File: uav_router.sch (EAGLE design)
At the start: 6 parts

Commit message: ???
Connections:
- net GND: now also U$1.VSS
- net OSC1: now also Y1.1
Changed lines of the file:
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@@
 <instance part="SUPPLY2" gate="G$1" x="55.88" y="86.36"/>
 <instance part="SUPPLY3" gate="G$1" x="144.78" y="73.66"/>
-<instance part="SUPPLY4" gate="G$1" x="96.52" y="91.44"/>
-<instance part="SUPPLY5" gate="G$1" x="78.74" y="93.98"/>
-<instance part="SUPPLY6" gate="G$1" x="78.74" y="91.44"/>
+<instance part="SUPPLY4" gate="G$1" x="86.36" y="116.84"/>
+<instance part="SUPPLY5" gate="G$1" x="88.9" y="116.84"/>
+<instance part="SUPPLY6" gate="G$1" x="83.82" y="116.84"/>
 <instance part="SUPPLY7" gate="G$1" x="111.76" y="76.2"/>
 <instance part="GND1" gate="1" x="27.94" y="27.94"/>
-<instance part="GND2" gate="1" x="114.3" y="111.76"/>
-<instance part="GND3" gate="1" x="104.14" y="104.14"/>
+<instance part="GND2" gate="1" x="104.14" y="119.38"/>
+<instance part="GND3" gate="1" x="50.8" y="27.94"/>
 <instance part="GND4" gate="1" x="142.24" y="27.94"/>
 <instance part="GND5" gate="1" x="142.24" y="43.18"/>
@@
 <wire x1="33.02" y1="27.94" x2="33.02" y2="91.44" width="0.762" layer="92"/>
 <wire x1="33.02" y1="91.44" x2="35.56" y2="93.98" width="0.762" layer="92"/>
-<wire x1="35.56" y1="93.98" x2="50.8" y2="93.98" width="0.762" layer="92"/>
-<wire x1="50.8" y1="93.98" x2="114.3" y2="93.98" width="0.762" layer="92"/>
+<wire x1="35.56" y1="93.98" x2="48.26" y2="93.98" width="0.762" layer="92"/>
+<wire x1="48.26" y1="93.98" x2="114.3" y2="93.98" width="0.762" layer="92"/>
 <wire x1="114.3" y1="93.98" x2="116.84" y2="91.44" width="0.762" layer="92"/>
-<wire x1="50.8" y1="93.98" x2="48.26" y2="91.44" width="0.762" layer="92"/>
-<wire x1="48.26" y1="91.44" x2="48.26" y2="27.94" width="0.762" layer="92"/>
+<wire x1="48.26" y1="93.98" x2="45.72" y2="91.44" width="0.762" layer="92"/>
+<wire x1="45.72" y1="91.44" x2="45.72" y2="27.94" width="0.762" layer="92"/>
 <wire x1="116.84" y1="91.44" x2="116.84" y2="27.94" width="0.762" layer="92"/>
 <wire x1="114.3" y1="93.98" x2="177.8" y2="93.98" width="0.762" layer="92"/>
@@
 <pinref part="SUPPLY7" gate="G$1" pin="3.3V"/>
 <wire x1="111.76" y1="50.8" x2="111.76" y2="76.2" width="0.1524" layer="91"/>
+<label x="101.6" y="50.8" size="1.778" layer="95"/>
 </segment>
 <segment>
@@
 <pinref part="GND6" gate="1" pin="GND"/>
 <wire x1="111.76" y1="48.26" x2="111.76" y2="30.48" width="0.1524" layer="91"/>
+<label x="101.6" y="48.26" size="1.778" layer="95"/>
 </segment>
 <segment>
@@
 <wire x1="149.86" y1="33.02" x2="142.24" y2="33.02" width="0.1524" layer="91"/>
 <wire x1="142.24" y1="33.02" x2="142.24" y2="30.48" width="0.1524" layer="91"/>
+</segment>
+<segment>
+<pinref part="U$1" gate="G$1" pin="VSS"/>
+<wire x1="60.96" y1="53.34" x2="50.8" y2="53.34" width="0.1524" layer="91"/>
+<wire x1="50.8" y1="53.34" x2="50.8" y2="30.48" width="0.1524" layer="91"/>
+<pinref part="GND3" gate="1" pin="GND"/>
+<label x="53.34" y="53.34" size="1.778" layer="95"/>
 </segment>
 </net>
@@
 <segment>
 <pinref part="U$1" gate="G$1" pin="OSC2"/>
-<wire x1="60.96" y1="48.26" x2="50.8" y2="48.26" width="0.1524" layer="91"/>
-<wire x1="50.8" y1="48.26" x2="48.26" y2="50.8" width="0.1524" layer="91"/>
+<wire x1="60.96" y1="48.26" x2="48.26" y2="48.26" width="0.1524" layer="91"/>
+<wire x1="48.26" y1="48.26" x2="45.72" y2="50.8" width="0.1524" layer="91"/>
 <label x="53.34" y="48.26" size="1.778" layer="95"/>
 </segment>
@@
 <segment>
 <pinref part="U$1" gate="G$1" pin="OSC1"/>
-<wire x1="60.96" y1="50.8" x2="50.8" y2="50.8" width="0.1524" layer="91"/>
-<wire x1="50.8" y1="50.8" x2="48.26" y2="53.34" width="0.1524" layer="91"/>
+<wire x1="60.96" y1="50.8" x2="48.26" y2="50.8" width="0.1524" layer="91"/>
+<wire x1="48.26" y1="50.8" x2="45.72" y2="53.34" width="0.1524" layer="91"/>
 <label x="53.34" y="50.8" size="1.778" layer="95"/>
 </segment>
@@
 <wire x1="177.8" y1="35.56" x2="180.34" y2="38.1" width="0.1524" layer="91"/>
 <label x="165.1" y="35.56" size="1.778" layer="95"/>
-</segment>
-</net>
+<pinref part="Y1" gate="G$1" pin="1"/>
+</segment>
+</net>

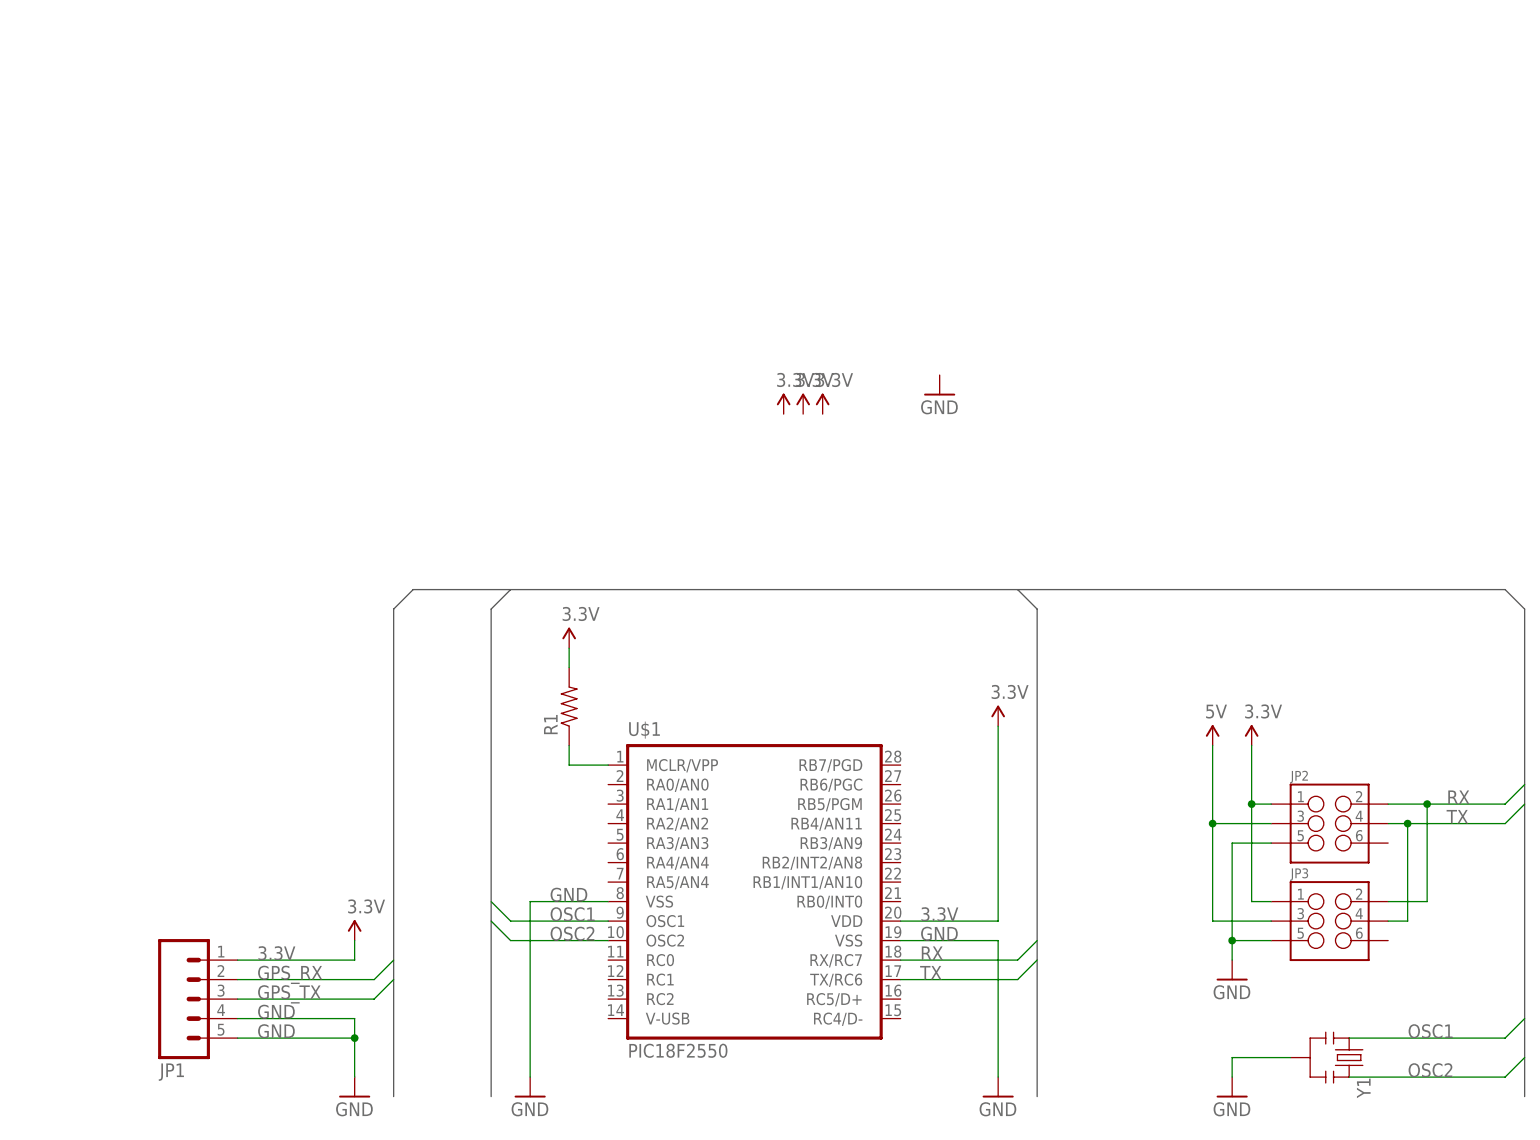
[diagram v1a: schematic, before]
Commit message: Adding GSM controller https://www.sparkfun.com/products/10497 and https://www.sparkfun.com/products/10138
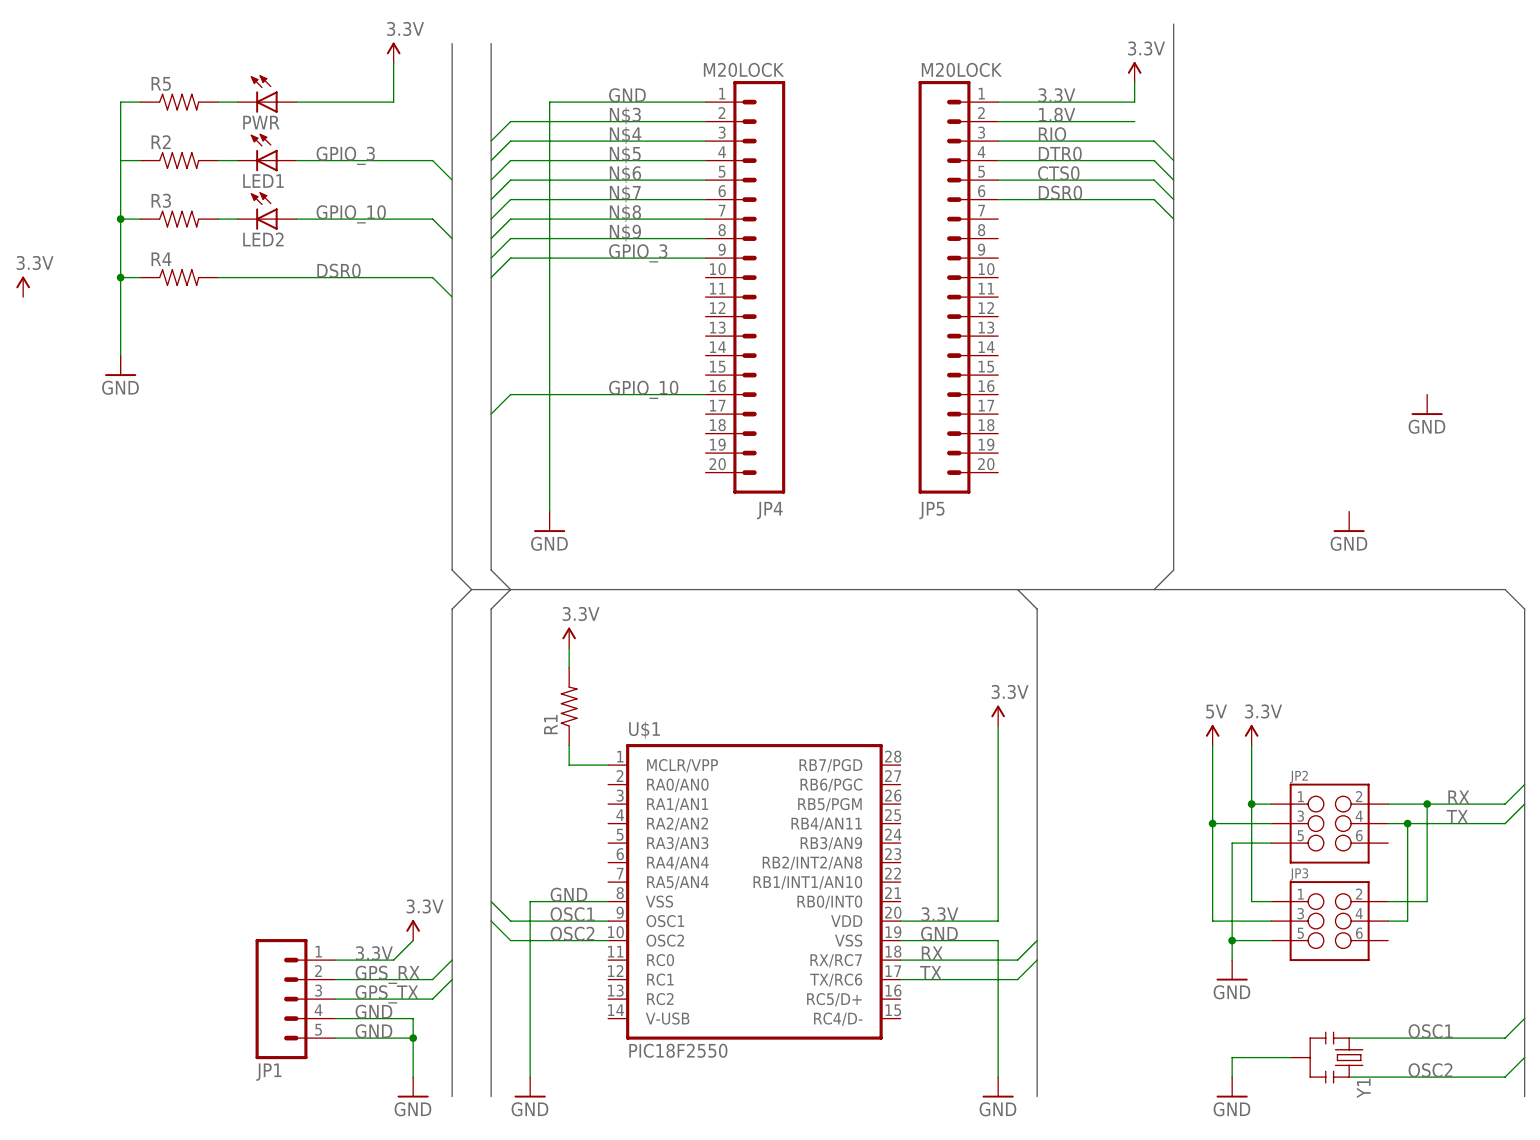
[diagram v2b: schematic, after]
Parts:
- added JP4, JP5: M20LOCK, SparkFun-Connectors:M20LOCK
- added LED1, LED2, PWR: (no value), SparkFun-LED:LED5MM
- added R2, R3, R4, R5: (no value), SparkFun-Resistors:RESISTORKIT
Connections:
- new net 1.8V: JP5.2
- new net CTS0: JP5.5
- new net DSR0: JP5.6, R4.2
- new net DTR0: JP5.4
- new net GPIO_10: JP4.16, LED2.A
- new net GPIO_3: JP4.9, LED1.A
- new net N$10: LED2.C, R3.2
- new net N$11: PWR.C, R5.2
- new net N$2: LED1.C, R2.2
- new net N$3: JP4.2
- new net N$4: JP4.3
- new net N$5: JP4.4
- new net N$6: JP4.5
- new net N$7: JP4.6
- new net N$8: JP4.7
- new net N$9: JP4.8
- new net RIO: JP5.3
- net 3.3V: now also JP5.1, PWR.A
- net GND: now also JP4.1, R2.1, R3.1, R4.1, R5.1
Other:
- moved on the sheet: JP1

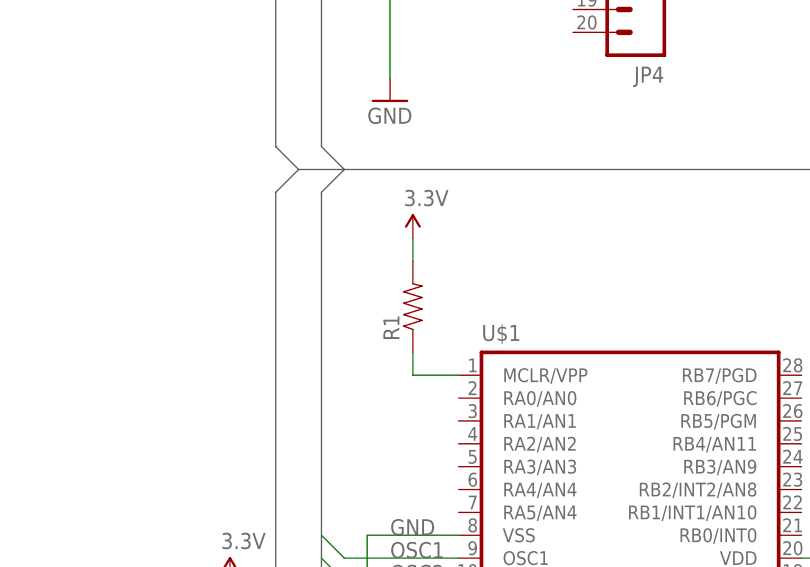
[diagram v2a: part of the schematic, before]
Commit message: Adding MCLR
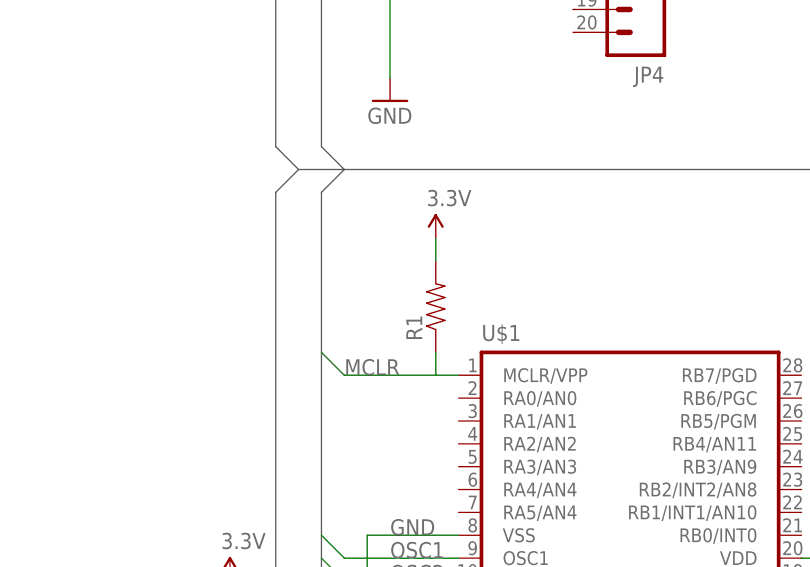
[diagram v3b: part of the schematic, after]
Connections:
- net N$1 renamed MCLR
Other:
- moved on the sheet: R1
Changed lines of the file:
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@@
 <instance part="JP1" gate="G$1" x="17.78" y="40.64" rot="MR180"/>
 <instance part="SUPPLY1" gate="G$1" x="35.56" y="48.26"/>
-<instance part="SUPPLY2" gate="G$1" x="55.88" y="86.36"/>
+<instance part="SUPPLY2" gate="G$1" x="58.42" y="86.36"/>
 <instance part="SUPPLY3" gate="G$1" x="144.78" y="73.66"/>
 <instance part="SUPPLY4" gate="G$1" x="129.54" y="160.02"/>
@@
 <instance part="JP3" gate="G$1" x="154.94" y="50.8"/>
 <instance part="SUPPLY8" gate="G$1" x="139.7" y="73.66"/>
-<instance part="R1" gate="G$1" x="55.88" y="78.74" rot="R90"/>
+<instance part="R1" gate="G$1" x="58.42" y="78.74" rot="R90"/>
 <instance part="Y1" gate="G$1" x="157.48" y="33.02" rot="R270"/>
 <instance part="JP4" gate="G$1" x="83.82" y="162.56" rot="R180"/>
@@
 <pinref part="R1" gate="G$1" pin="2"/>
 <pinref part="SUPPLY2" gate="G$1" pin="3.3V"/>
-<wire x1="55.88" y1="83.82" x2="55.88" y2="86.36" width="0.1524" layer="91"/>
+<wire x1="58.42" y1="83.82" x2="58.42" y2="86.36" width="0.1524" layer="91"/>
 </segment>
 <segment>
@@
 </segment>
 </net>
-<net name="N$1" class="0">
+<net name="MCLR" class="0">
 <segment>
 <pinref part="U$1" gate="G$1" pin="MCLR/VPP"/>
 <pinref part="R1" gate="G$1" pin="1"/>
-<wire x1="60.96" y1="71.12" x2="55.88" y2="71.12" width="0.1524" layer="91"/>
-<wire x1="55.88" y1="71.12" x2="55.88" y2="73.66" width="0.1524" layer="91"/>
-</segment>
-</net>
+<wire x1="60.96" y1="71.12" x2="58.42" y2="71.12" width="0.1524" layer="91"/>
+<wire x1="58.42" y1="71.12" x2="58.42" y2="73.66" width="0.1524" layer="91"/>
+<wire x1="58.42" y1="71.12" x2="48.26" y2="71.12" width="0.1524" layer="91"/>
+<wire x1="48.26" y1="71.12" x2="45.72" y2="73.66" width="0.1524" layer="91"/>
+<label x="48.26" y="71.12" size="1.778" layer="95"/>
+</segment>
+</net>

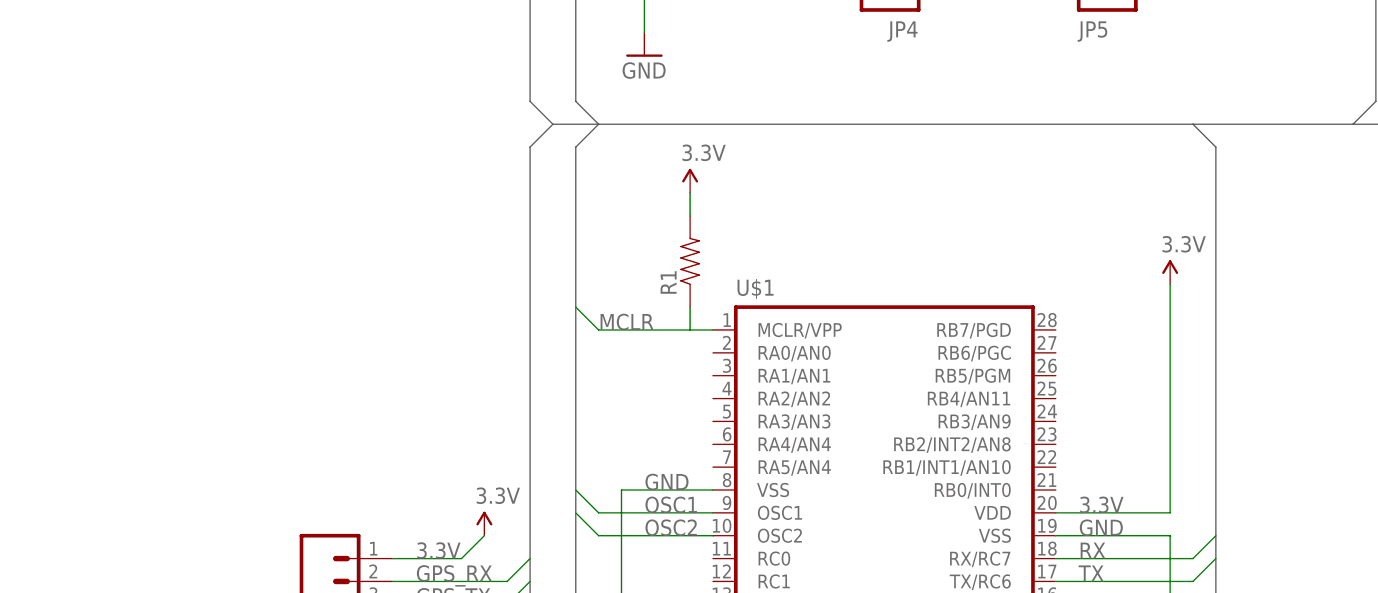
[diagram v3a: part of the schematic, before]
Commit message: Adding ICSP programming interface
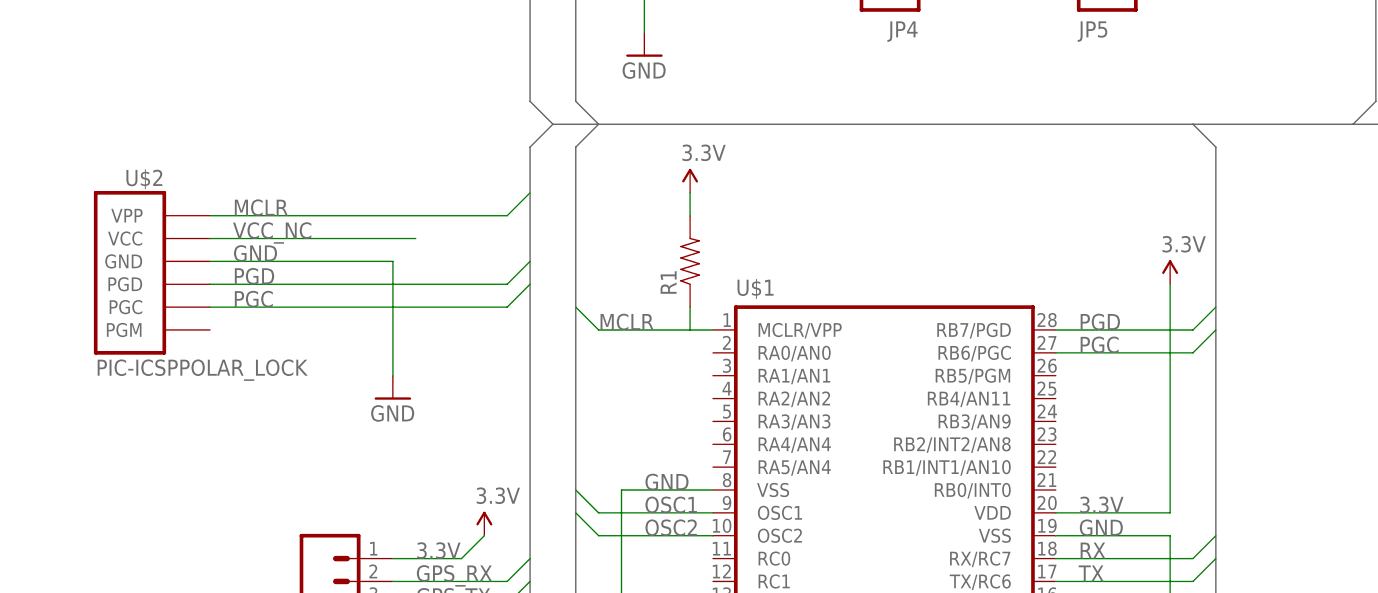
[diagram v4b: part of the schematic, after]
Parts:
- added U$2: PIC-ICSPPOLAR_LOCK, SparkFun-Connectors:PIC-ICSPPOLAR_LOCK
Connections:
- new net PGC: U$1.RB6/PGC, U$2.PGC
- new net PGD: U$1.RB7/PGD, U$2.PGD
- new net VCC_NC: U$2.VCC
- net GND: now also U$2.GND
- net MCLR: now also U$2.VPP
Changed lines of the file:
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@@
 <part name="R5" library="SparkFun-Resistors" deviceset="RESISTOR" device="KIT"/>
 <part name="PWR" library="SparkFun-LED" deviceset="LED" device="5MM"/>
+<part name="U$2" library="SparkFun-Connectors" deviceset="PIC-ICSP" device="POLAR_LOCK"/>
+<part name="GND10" library="SparkFun-Aesthetics" deviceset="GND" device=""/>
 </parts>
 <sheets>
@@
 <instance part="R5" gate="G$1" x="5.08" y="157.48"/>
 <instance part="PWR" gate="G$1" x="17.78" y="157.48" rot="R270"/>
+<instance part="U$2" gate="G$1" x="-2.54" y="78.74"/>
+<instance part="GND10" gate="1" x="25.4" y="63.5"/>
 </instances>
 <busses>
@@
 <wire x1="-2.54" y1="157.48" x2="0" y2="157.48" width="0.1524" layer="91"/>
 </segment>
+<segment>
+<pinref part="U$2" gate="G$1" pin="GND"/>
+<pinref part="GND10" gate="1" pin="GND"/>
+<wire x1="5.08" y1="78.74" x2="25.4" y2="78.74" width="0.1524" layer="91"/>
+<wire x1="25.4" y1="78.74" x2="25.4" y2="66.04" width="0.1524" layer="91"/>
+<label x="7.62" y="78.74" size="1.778" layer="95"/>
+</segment>
 </net>
 <net name="5V" class="0">
@@
 <label x="48.26" y="71.12" size="1.778" layer="95"/>
 </segment>
+<segment>
+<pinref part="U$2" gate="G$1" pin="VPP"/>
+<wire x1="5.08" y1="83.82" x2="38.1" y2="83.82" width="0.1524" layer="91"/>
+<wire x1="38.1" y1="83.82" x2="40.64" y2="86.36" width="0.1524" layer="91"/>
+<label x="7.62" y="83.82" size="1.778" layer="95"/>
+</segment>
 </net>
 <net name="OSC2" class="0">
@@
 </segment>
 </net>
+<net name="VCC_NC" class="0">
+<segment>
+<pinref part="U$2" gate="G$1" pin="VCC"/>
+<wire x1="5.08" y1="81.28" x2="27.94" y2="81.28" width="0.1524" layer="91"/>
+<label x="7.62" y="81.28" size="1.778" layer="95"/>
+</segment>
+</net>
+<net name="PGD" class="0">
+<segment>
+<pinref part="U$2" gate="G$1" pin="PGD"/>
+<wire x1="5.08" y1="76.2" x2="38.1" y2="76.2" width="0.1524" layer="91"/>
+<wire x1="38.1" y1="76.2" x2="40.64" y2="78.74" width="0.1524" layer="91"/>
+<label x="7.62" y="76.2" size="1.778" layer="95"/>
+</segment>
+<segment>
+<pinref part="U$1" gate="G$1" pin="RB7/PGD"/>
+<wire x1="99.06" y1="71.12" x2="114.3" y2="71.12" width="0.1524" layer="91"/>
+<wire x1="114.3" y1="71.12" x2="116.84" y2="73.66" width="0.1524" layer="91"/>
+<label x="101.6" y="71.12" size="1.778" layer="95"/>
+</segment>
+</net>
+<net name="PGC" class="0">
+<segment>
+<pinref part="U$2" gate="G$1" pin="PGC"/>
+<wire x1="5.08" y1="73.66" x2="38.1" y2="73.66" width="0.1524" layer="91"/>
+<wire x1="38.1" y1="73.66" x2="40.64" y2="76.2" width="0.1524" layer="91"/>
+<label x="7.62" y="73.66" size="1.778" layer="95"/>
+</segment>
+<segment>
+<pinref part="U$1" gate="G$1" pin="RB6/PGC"/>
+<wire x1="99.06" y1="68.58" x2="114.3" y2="68.58" width="0.1524" layer="91"/>
+<wire x1="114.3" y1="68.58" x2="116.84" y2="71.12" width="0.1524" layer="91"/>
+<label x="101.6" y="68.58" size="1.778" layer="95"/>
+</segment>
+</net>
